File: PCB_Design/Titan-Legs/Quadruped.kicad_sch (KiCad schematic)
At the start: 36 parts

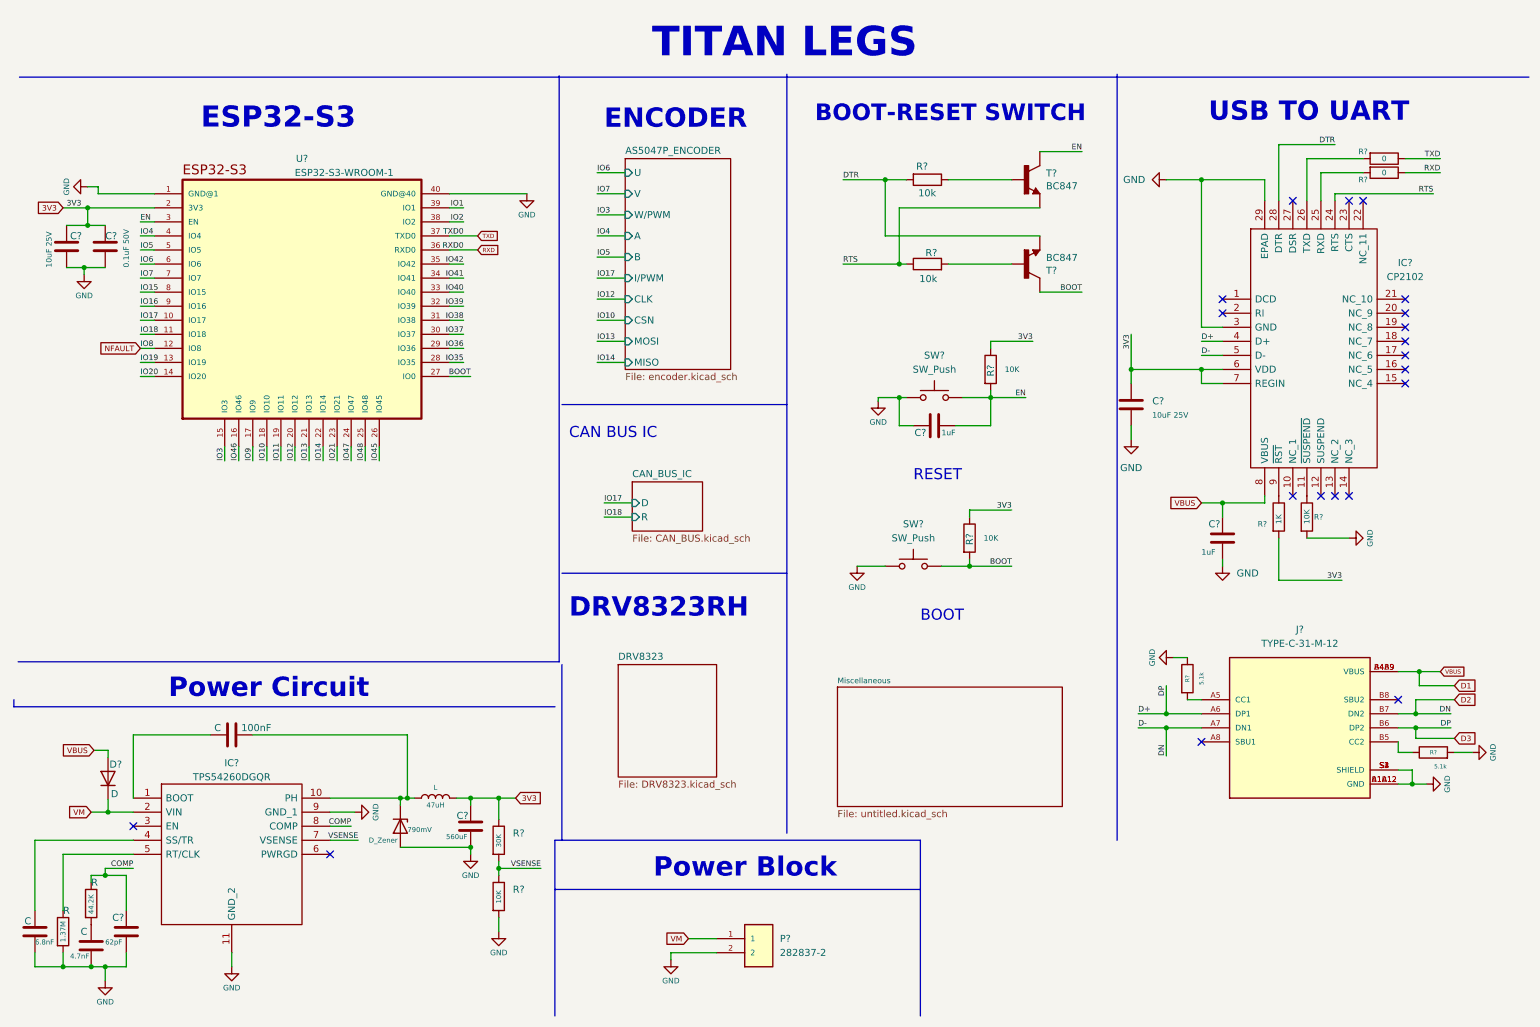
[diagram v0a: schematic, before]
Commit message: schematics 1st iteration completed
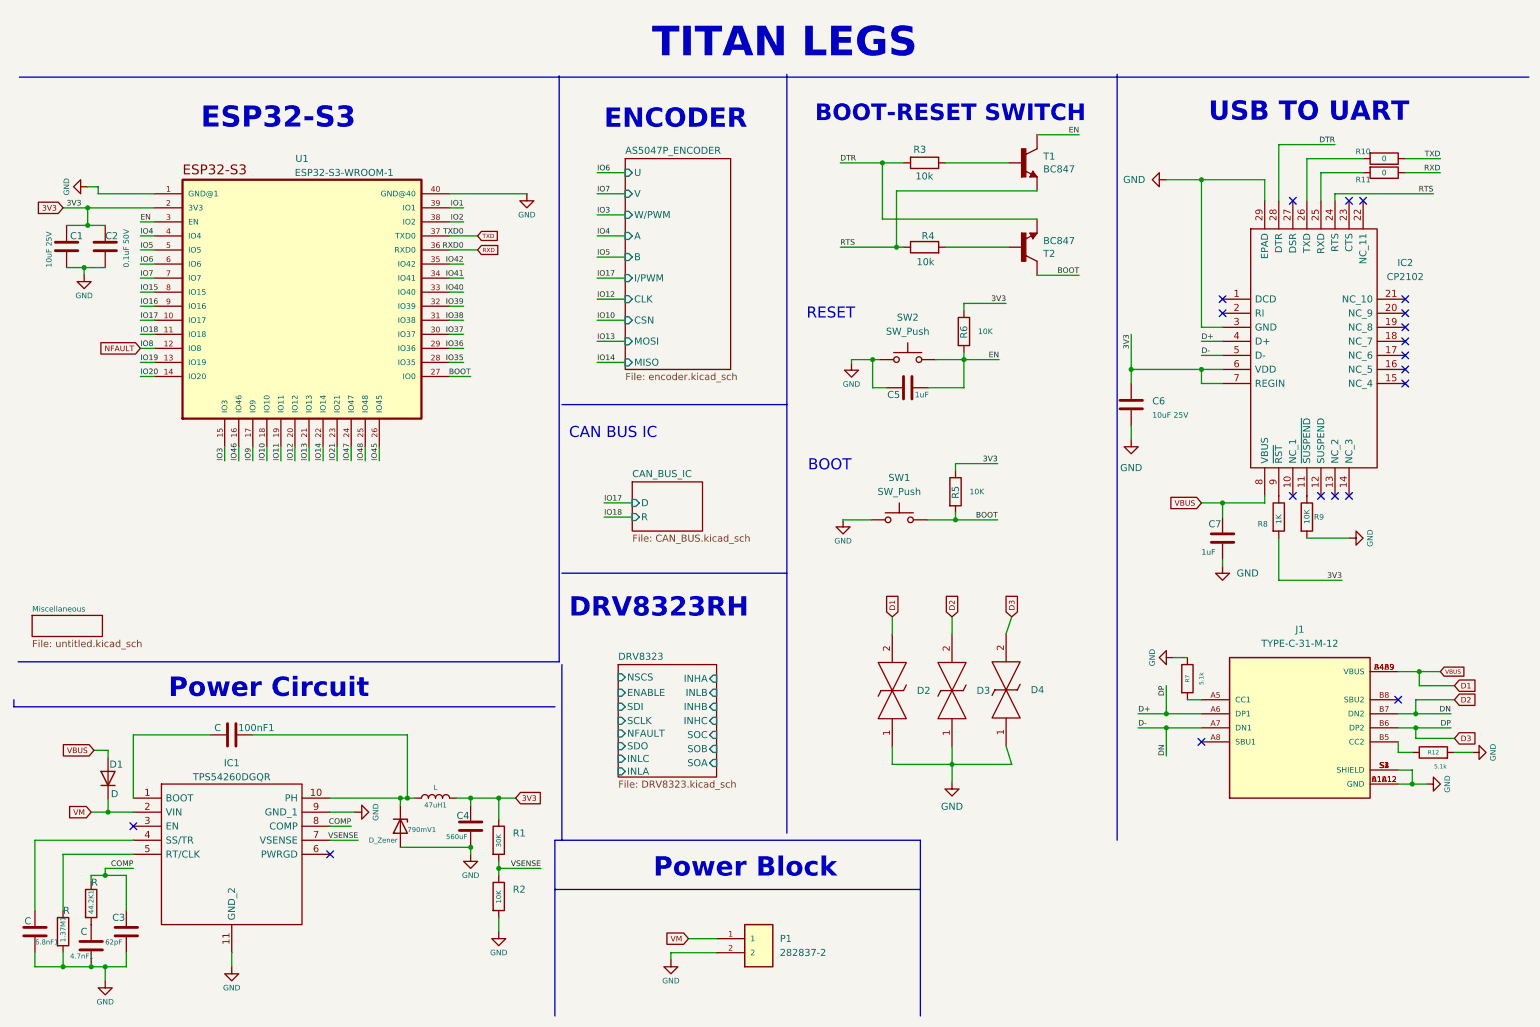
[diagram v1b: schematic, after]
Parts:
- added D2, D3, D4: LESD5D5.0CT1G, LESD5D50CT1G, symbol USB-UART_LESD5D5.0CT1G:LESD5D5.0CT1G
- gave numbers to parts that had none: 29
- renumbered 1.37M to 1.37M1, 100nF to 100nF1, 4.7nF to 4.7nF1, 44.2K to 44.2K1, 47uH to 47uH1, 6.8nF to 6.8nF1, 790mV to 790mV1
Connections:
- net D1: now also D2.2
- net D2: now also D3.2
- net D3: now also D4.2
- net GND: now also D2.1, D3.1, D4.1
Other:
- sheet DRV8323 ports: added ENABLE, INHA, INHB, INHC, INLA, INLB, INLC, NFAULT, NSCS, SCLK, SDI, SDO, SOA, SOB, SOC; removed none
- moved on the sheet: C5, R3, R4, R5, R6, SW1, SW2, T1, T2

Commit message: Schematics 2nd Iteration Completed
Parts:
- added R?: 47.5K, LED_SMD:LED_0603_1608Metric, symbol Device:R
- added R?: 22.1K, LED_SMD:LED_0603_1608Metric, symbol Device:R
- C7: value 1uF -> 1uF 16V
- renumbered 1.37M1 to 1.37M, 100nF1 to 100nF, 4.7nF1 to 4.7nF, 44.2K1 to 44.2K, 47uH1 to 47uH, 6.8nF1 to 6.8nF, 790mV1 to 790mV
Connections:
- net GND: now also R?.2
- net D1 renamed VBUS
- net VBUS: now also R?.1; no longer C7.1, IC2.8 (VBUS)
- net D2 renamed D-
- net D3 renamed D+
- net NFAULT renamed IO8
- new net: C7.1, IC2.8 (VBUS), R?.1, R?.2
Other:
- moved on the sheet: D4

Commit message: Added AMS1117 for ESP32-S3
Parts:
- added C25, C27: 10uF 25V, symbol Device:C
- added C26, C28: 0.1uF 50V, symbol Device:C
- added U4: AMS1117-3.3, SOT229P700X180-4N, symbol AMS1117-3.3:AMS1117-3.3
- gave numbers to parts that had none: 2
- renumbered 1.37M to 1.37M1, 100nF to 100nF1, 4.7nF to 4.7nF1, 44.2K to 44.2K1, 47uH to 47uH1, 6.8nF to 6.8nF1, 790mV to 790mV1
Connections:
- net GND: now also C25.2, C26.2, C27.2, C28.2, U4.1 (GND/ADJ)
- net VBUS: now also C25.1, C26.1, U4.3 (VIN); no longer D1.2 (A)
- net VM: no longer D1.1 (K)
- net 3V3 renamed 3V3_IN
- net 3V3_IN: now also D1.1 (K)
- net IO15: no longer names the net of U1.8 (IO15)
- net IO16: no longer names the net of U1.9 (IO16)
- net IO20: no longer names the net of U1.14 (IO20)
- net IO3: no longer names the net of U1.15 (IO3)
- net IO35: no longer names the net of U1.28 (IO35)
- net IO42: no longer names the net of U1.35 (IO42)
- net IO45: no longer names the net of U1.26 (IO45)
- net IO46: no longer names the net of U1.16 (IO46)
- new net ESP_3V3: C27.1, C28.1, D1.2 (A), U4.2 (VOUT)
- no-connect marks 20 -> 28
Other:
- sheet AS5047P_ENCODER ports: added 3V3; removed none
- sheet CAN_BUS_IC ports: added 3V3; removed none
- sheet DRV8323 ports: added 3V3; removed none

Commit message: updated minor changes
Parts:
- renumbered 1.37M1 to 1.37M, 100nF1 to 100nF, 4.7nF1 to 4.7nF, 44.2K1 to 44.2K, 47uH1 to 47uH, 6.8nF1 to 6.8nF, 790mV1 to 790mV
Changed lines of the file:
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@@
     (stroke (width 0) (type default) (color 0 0 0 0))
   )
-  (wire (pts (xy 99.06 158.75) (xy 104.394 158.75))
+  (wire (pts (xy 99.06 158.75) (xy 106.934 158.75))
     (stroke (width 0) (type default) (color 0 0 0 0))
   )
@@
     (stroke (width 0) (type default) (color 0 0 0 0))
   )
-  (wire (pts (xy 99.06 171.45) (xy 106.68 171.45))
+  (wire (pts (xy 99.06 171.45) (xy 108.2548 171.45))
     (stroke (width 0) (type default) (color 0 0 0 0))
   )
@@
     (effects (font (size 3.5 3.5) bold) (justify left bottom))
   )
-  (text "ESP32-S3" (at 45.212 38.1 0)
+  (text "ESP32-S3" (at 45.72 37.846 0)
     (effects (font (size 3.81 3.81) (thickness 0.762) bold) (justify left bottom))
   )
@@
     (effects (font (size 1 1)) (justify right bottom))
   )
-  (label "VSENSE" (at 106.68 171.45 180)
+  (label "VSENSE" (at 108.2548 171.45 180)
     (effects (font (size 1 1)) (justify right bottom))
   )
@@
     (effects (font (size 1 1)) (justify left bottom))
   )
-  (label "3V3" (at 104.394 158.75 180)
+  (label "3V3" (at 106.934 158.75 180)
     (effects (font (size 1 1)) (justify right bottom))
   )
@@
   (symbol (lib_id "Device:C") (at 15.24 182.88 0) (unit 1)
     (in_bom yes) (on_board yes)
-    (property "Reference" "6.8nF1" (id 0) (at 15.24 184.785 0)
+    (property "Reference" "6.8nF" (id 0) (at 15.24 184.785 0)
       (effects (font (size 0.9 0.9)) (justify left))
     )
@@
   (symbol (lib_id "Device:L") (at 87.63 158.75 90) (unit 1)
     (in_bom yes) (on_board yes)
-    (property "Reference" "47uH1" (id 0) (at 87.63 160.02 90)
+    (property "Reference" "47uH" (id 0) (at 87.63 160.02 90)
       (effects (font (size 0.9 0.9)))
     )
@@
   (symbol (lib_id "Device:R") (at 25.4 177.8 0) (unit 1)
     (in_bom yes) (on_board yes)
-    (property "Reference" "44.2K1" (id 0) (at 25.4 179.705 90)
+    (property "Reference" "44.2K" (id 0) (at 25.4 179.705 90)
       (effects (font (size 0.9 0.9)) (justify left))
     )
@@
   (symbol (lib_id "Device:R") (at 20.32 182.88 0) (unit 1)
     (in_bom yes) (on_board yes)
-    (property "Reference" "1.37M1" (id 0) (at 20.32 184.785 90)
+    (property "Reference" "1.37M" (id 0) (at 20.32 184.785 90)
       (effects (font (size 0.9 0.9)) (justify left))
     )
@@
   (symbol (lib_id "Device:C") (at 25.4 185.42 0) (unit 1)
     (in_bom yes) (on_board yes)
-    (property "Reference" "4.7nF1" (id 0) (at 21.59 187.325 0)
+    (property "Reference" "4.7nF" (id 0) (at 21.59 187.325 0)
       (effects (font (size 0.9 0.9)) (justify left))
     )
@@
   (symbol (lib_id "Device:R") (at 223.52 137.16 0) (unit 1)
     (in_bom yes) (on_board yes)
-    (property "Reference" "R7" (id 0) (at 223.52 137.16 90)
-      (effects (font (size 0.762 0.762)))
-    )
-    (property "Value" "5.1k" (id 1) (at 226.06 137.16 90)
-      (effects (font (size 0.762 0.762)))
+    (property "Reference" "R7" (id 0) (at 226.0092 136.9568 0)
+      (effects (font (size 1 1)))
+    )
+    (property "Value" "5.1k" (id 1) (at 223.52 136.906 90)
+      (effects (font (size 1 1)))
     )
     (property "Footprint" "" (id 2) (at 221.742 137.16 90)
@@
   (symbol (lib_id "Device:R") (at 224.536 111.76 0) (unit 1)
     (in_bom yes) (on_board yes)
-    (property "Reference" "R22" (id 0) (at 221.488 111.76 0)
+    (property "Reference" "R22" (id 0) (at 220.472 111.76 0)
       (effects (font (size 1 1)) (justify left))
     )
@@
   (symbol (lib_id "Device:C") (at 50.8 147.32 90) (unit 1)
     (in_bom yes) (on_board yes)
-    (property "Reference" "100nF1" (id 0) (at 55.245 146.05 90))
+    (property "Reference" "100nF" (id 0) (at 55.245 146.05 90)
+      (effects (font (size 1 1)))
+    )
     (property "Value" "C" (id 1) (at 48.26 146.05 90))
     (property "Footprint" "" (id 2) (at 54.61 146.3548 0)
@@
   (symbol (lib_id "Device:D_Zener") (at 81.28 163.83 270) (unit 1)
     (in_bom yes) (on_board yes)
-    (property "Reference" "790mV1" (id 0) (at 82.55 164.465 90)
+    (property "Reference" "790mV" (id 0) (at 82.55 164.465 90)
       (effects (font (size 0.9 0.9)) (justify left))
     )
@@
     )
     (path "/685b7ea4-0e36-4b4e-98e9-e356cbba78be"
-      (reference "1.37M1") (unit 1) (value "R") (footprint "")
+      (reference "1.37M") (unit 1) (value "R") (footprint "")
     )
     (path "/87c3190e-061f-4f9c-a1ca-aba226149746"
-      (reference "4.7nF1") (unit 1) (value "C") (footprint "")
+      (reference "4.7nF") (unit 1) (value "C") (footprint "")
     )
     (path "/24520828-dfe4-497d-beb1-9ab47b76cfd9"
-      (reference "6.8nF1") (unit 1) (value "C") (footprint "")
+      (reference "6.8nF") (unit 1) (value "C") (footprint "")
     )
     (path "/330798c7-b394-4252-9d51-491e7cc66c14"
-      (reference "44.2K1") (unit 1) (value "R") (footprint "")
+      (reference "44.2K") (unit 1) (value "R") (footprint "")
     )
     (path "/32bf2d91-ca5e-4e05-87bc-9c7a4f82f965"
-      (reference "47uH1") (unit 1) (value "L") (footprint "")
+      (reference "47uH") (unit 1) (value "L") (footprint "")
     )
     (path "/c7f3643e-89ab-411f-a380-20e102da59ad"
-      (reference "100nF1") (unit 1) (value "C") (footprint "")
+      (reference "100nF") (unit 1) (value "C") (footprint "")
     )
     (path "/fddf2939-6581-4168-83e6-bfc5e62b7a8a"
-      (reference "790mV1") (unit 1) (value "D_Zener") (footprint "")
+      (reference "790mV") (unit 1) (value "D_Zener") (footprint "")
     )
     (path "/3d4bb42d-446b-459c-b3a9-3f02c158a450"

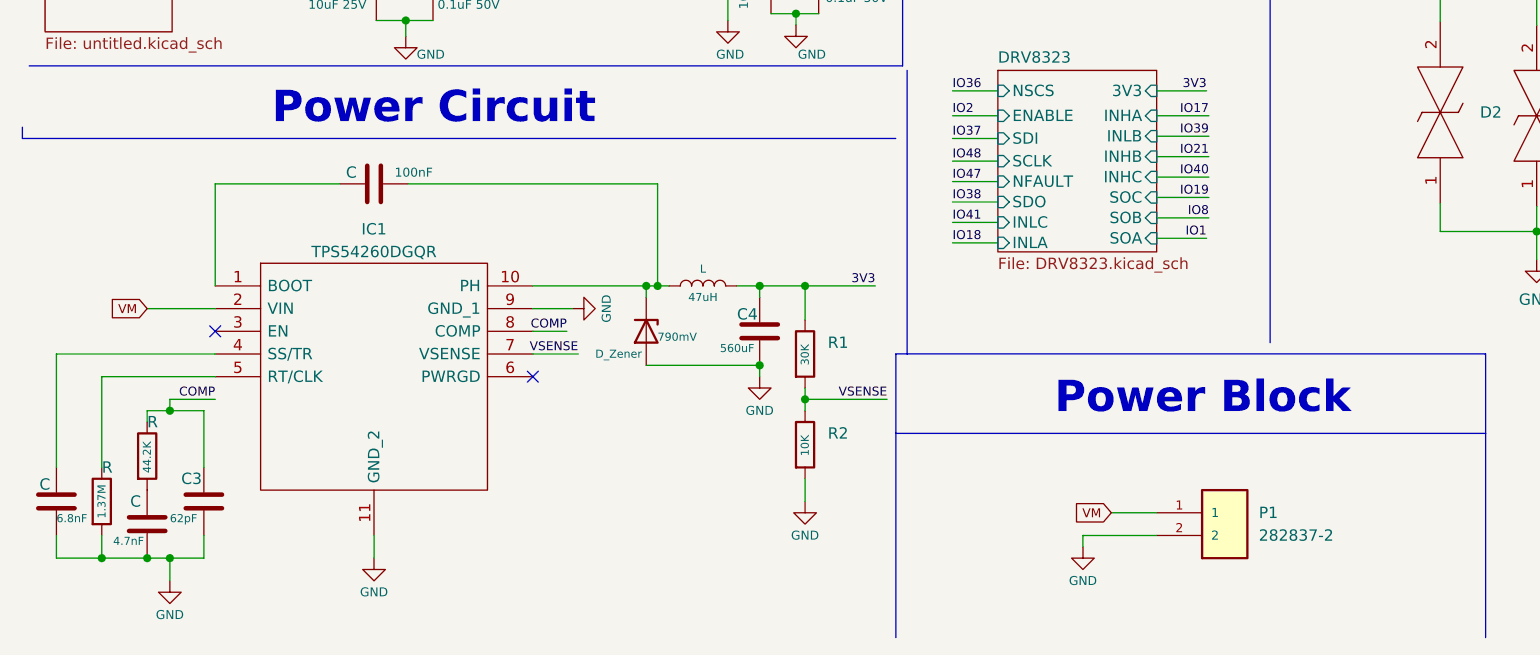
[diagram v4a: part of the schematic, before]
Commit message: added electrolytic capacitors
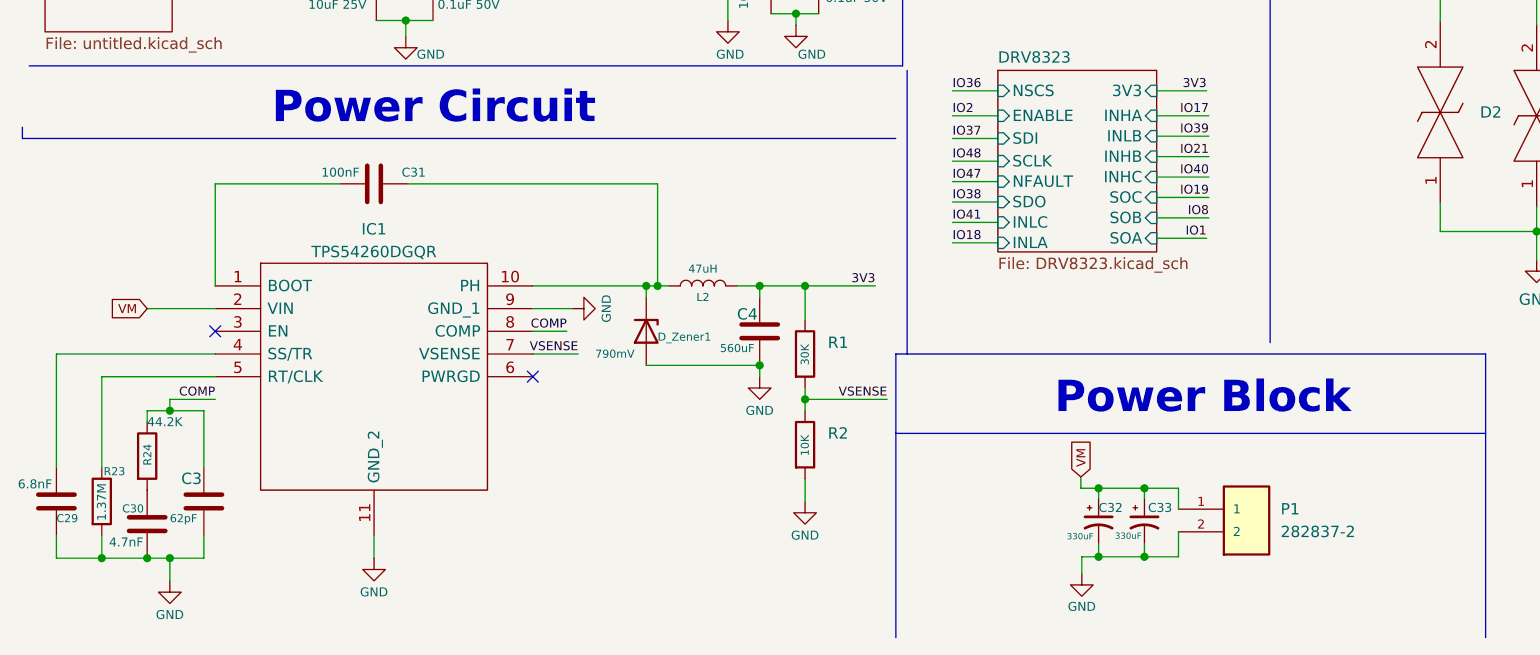
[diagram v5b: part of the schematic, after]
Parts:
- added C32, C33: 330uF, Capacitor_SMD:CP_Elec_8x10, symbol Device:C_Polarized_Small_US
- C1, C2, C25, C26, C27, C28, C3, C4, C5, C6: footprint (none) -> Capacitor_SMD:C_0603_1608Metric
- C29: renamed from 6.8nF; value C -> 6.8nF; footprint (none) -> Capacitor_SMD:C_0603_1608Metric
- C30: renamed from 4.7nF; value C -> 4.7nF; footprint (none) -> Capacitor_SMD:C_0603_1608Metric
- C31: renamed from 100nF; value C -> 100nF; footprint (none) -> Capacitor_SMD:C_0603_1608Metric
- D_Zener1: renamed from 790mV; value D_Zener -> 790mV
- IC1: footprint SOP50P490X110-11N -> Buck Converter:IC_XTR111AIDGQR
- J1: footprint HRO_TYPE-C-31-M-12 -> usb c:HRO_TYPE-C-31-M-12
- L2: renamed from 47uH; value L -> 47uH
- P1: footprint TE_282837-2 -> TerminalBlock:TerminalBlock_bornier-2_P5.08mm
- R2, R5, R6: footprint (none) -> Resistor_SMD:R_0603_1608Metric
- R21, R22, R8: footprint LED_SMD:LED_0603_1608Metric -> (none)
- R23: renamed from 1.37M; value R -> 1.37M
- R24: renamed from 44.2K; value R -> 44.2K
- R9: footprint LED_SMD:LED_0603_1608Metric -> Resistor_SMD:R_0603_1608Metric
- T1, T2: footprint BC847:BC847 -> BC847_BJT:SOT23
- U1: footprint ESP32-S3-WROOM-1 -> RF_Module:ESP32-S3-WROOM-1
- U4: footprint SOT229P700X180-4N -> AMS1117-3:SOT229P700X180-4N
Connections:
- net GND: now also C32.2, C33.2
- net VM: now also C32.1, C33.1
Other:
- moved on the sheet: P1

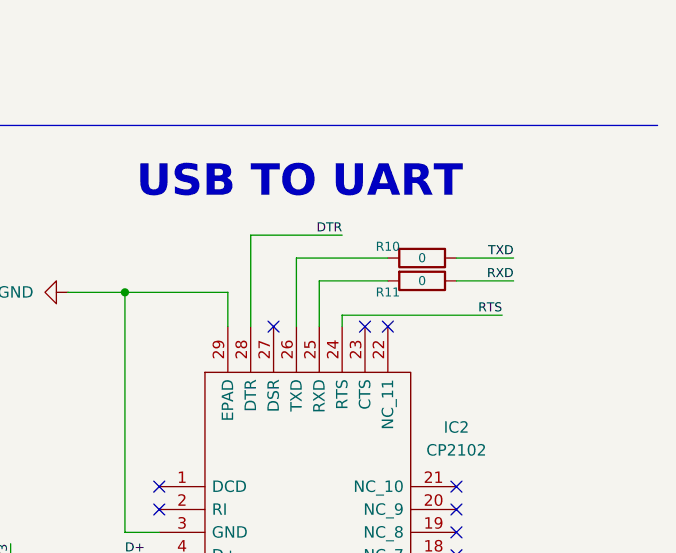
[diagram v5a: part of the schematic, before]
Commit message: footprint assignment done
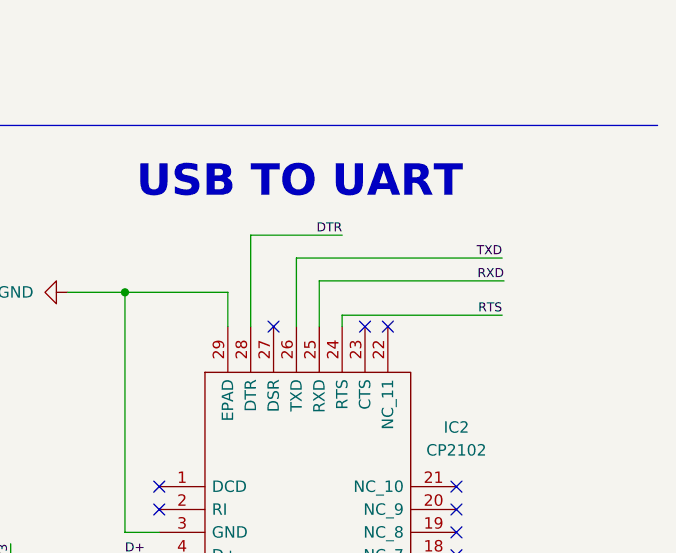
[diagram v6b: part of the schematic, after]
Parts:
- removed R10, R11: 0, symbol Device:R
- D1, D_Zener1: footprint (none) -> SS34:DIOM7959X265N
- D2, D3, D4: footprint LESD5D50CT1G -> LESD_diode:LESD5D50CT1G
- L2: footprint (none) -> Inductor_47uH:INDPM120120X800N
- R1, R12, R21, R22, R23, R24, R7, R8: footprint (none) -> Resistor_SMD:R_0603_1608Metric
- SW1, SW2: footprint (none) -> SW_TL1015AF160QG:SW_TL1015AF160QG
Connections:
- net RXD: now also IC2.25 (RXD)
- net TXD: now also IC2.26 (TXD)
